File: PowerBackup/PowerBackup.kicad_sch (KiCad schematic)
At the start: 0 parts

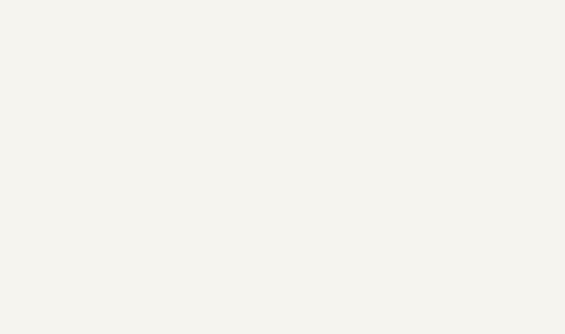
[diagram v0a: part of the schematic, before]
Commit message: Changed resistors and LEDs to 0805 and updated Production files
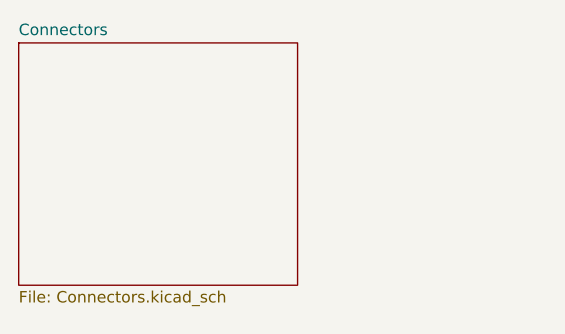
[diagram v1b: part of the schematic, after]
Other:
- added sheet Connectors (Connectors.kicad_sch)

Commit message: Did some initial board layout
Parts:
- added H1, H2, H3: MountingHole_Pad, MountingHole:MountingHole_2.7mm_M2.5_Pad, symbol Mechanical:MountingHole_Pad
- added J1: Conn_01x02_Female, Connector_JST:JST_XH_B2B-XH-A_1x02_P2.50mm_Vertical, symbol Connector:Conn_01x02_Female
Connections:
- new net +9V: J1.1 (Pin_1)
- new net GND: H1.1, H2.1, H3.1, J1.2 (Pin_2)
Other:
- removed sheet Connectors
- added sheet Backup (Backup.kicad_sch)

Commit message: Added BOM and production files
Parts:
- H1, H2, H3, J1: MFN# (none) -> -
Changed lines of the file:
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@@
     (stroke (width 0) (type default) (color 0 0 0 0))
+  )
+  (wire (pts (xy 23.876 127.762) (xy 31.242 127.762))
+    (stroke (width 0) (type default) (color 0 0 0 0))
+  )
+  (symbol (lib_id "power:PWR_FLAG") (at 23.876 127.762 0) (unit 1)
+    (in_bom yes) (on_board yes) (fields_autoplaced)
+    (property "Reference" "#FLG0101" (id 0) (at 23.876 125.857 0)
+      (effects (font (size 1.27 1.27)) hide)
+    )
+    (property "Value" "PWR_FLAG" (id 1) (at 23.876 123.19 0))
+    (property "Footprint" "" (id 2) (at 23.876 127.762 0)
+      (effects (font (size 1.27 1.27)) hide)
+    )
+    (property "Datasheet" "~" (id 3) (at 23.876 127.762 0)
+      (effects (font (size 1.27 1.27)) hide)
+    )
+    (pin "1")
   )
   (symbol (lib_id "power:GND") (at 31.242 34.29 0) (unit 1)
@@
     (pin "1")
   )
+  (symbol (lib_id "power:+9V") (at 31.242 127.762 0) (unit 1)
+    (in_bom yes) (on_board yes) (fields_autoplaced)
+    (property "Reference" "#PWR0104" (id 0) (at 31.242 131.572 0)
+      (effects (font (size 1.27 1.27)) hide)
+    )
+    (property "Value" "+9V" (id 1) (at 31.242 123.19 0))
+    (property "Footprint" "" (id 2) (at 31.242 127.762 0)
+      (effects (font (size 1.27 1.27)) hide)
+    )
+    (property "Datasheet" "" (id 3) (at 31.242 127.762 0)
+      (effects (font (size 1.27 1.27)) hide)
+    )
+    (pin "1")
+  )
   (symbol (lib_id "power:GND") (at 27.432 190.246 0) (unit 1)
     (in_bom yes) (on_board yes) (fields_autoplaced)
@@
       (effects (font (size 1.27 1.27)) hide)
     )
+    (property "MFN#" "-" (id 4) (at 34.798 186.69 0)
+      (effects (font (size 1.27 1.27)) hide)
+    )
     (pin "1")
   )
@@
       (effects (font (size 1.27 1.27)) hide)
     )
+    (property "MFN#" "-" (id 4) (at 44.196 31.496 0)
+      (effects (font (size 1.27 1.27)) hide)
+    )
     (pin "1")
     (pin "2")
@@
       (effects (font (size 1.27 1.27)) hide)
     )
+    (property "MFN#" "-" (id 4) (at 27.432 186.69 0)
+      (effects (font (size 1.27 1.27)) hide)
+    )
     (pin "1")
   )
@@
     )
     (property "Datasheet" "~" (id 3) (at 19.812 186.69 0)
+      (effects (font (size 1.27 1.27)) hide)
+    )
+    (property "MFN#" "-" (id 4) (at 19.812 186.69 0)
       (effects (font (size 1.27 1.27)) hide)
     )
@@
   )
   (symbol_instances
+    (path "/4b4f8a8e-03cf-40a7-8fad-fe39dfbabdac"
+      (reference "#FLG0101") (unit 1) (value "PWR_FLAG") (footprint "")
+    )
     (path "/68d26012-5170-4c8d-8ec1-a7d027a0af0d"
       (reference "#PWR01") (unit 1) (value "GND") (footprint "")
@@
       (reference "#PWR05") (unit 1) (value "GND") (footprint "")
     )
-    (path "/915b7dab-7a0a-46d7-be45-5545593eb525/ba36fb47-be2e-439c-8a56-c72c46503d6d"
-      (reference "#PWR06") (unit 1) (value "GNDS") (footprint "")
-    )
-    (path "/915b7dab-7a0a-46d7-be45-5545593eb525/69ac9631-ec7e-4f05-ba31-4e83c5dfbd90"
-      (reference "#PWR07") (unit 1) (value "GNDS") (footprint "")
-    )
-    (path "/915b7dab-7a0a-46d7-be45-5545593eb525/be06c08d-5421-4385-826b-8847f44af1cc"
-      (reference "#PWR08") (unit 1) (value "GNDS") (footprint "")
-    )
-    (path "/915b7dab-7a0a-46d7-be45-5545593eb525/a22b1e65-5405-474d-b1be-0a774a13d3fb"
-      (reference "#PWR09") (unit 1) (value "GNDS") (footprint "")
-    )
-    (path "/915b7dab-7a0a-46d7-be45-5545593eb525/18bf62f4-4ef8-4a56-84ab-efff4fd1d94e"
-      (reference "#PWR010") (unit 1) (value "GNDS") (footprint "")
-    )
-    (path "/915b7dab-7a0a-46d7-be45-5545593eb525/4b968b19-6208-4b08-9d76-2833cc577fde"
-      (reference "#PWR011") (unit 1) (value "GNDS") (footprint "")
-    )
-    (path "/915b7dab-7a0a-46d7-be45-5545593eb525/d05ba0a5-c00f-4110-935e-a1ec267428a9"
-      (reference "#PWR012") (unit 1) (value "GNDS") (footprint "")
-    )
     (path "/244de032-dfe4-4b77-a637-dbe4a930144c/5183010c-eb20-44ae-bdff-7b0ef9cbe2e0"
       (reference "#PWR013") (unit 1) (value "GND") (footprint "")
@@
       (reference "#PWR014") (unit 1) (value "+9VA") (footprint "")
     )
-    (path "/244de032-dfe4-4b77-a637-dbe4a930144c/982dd809-aff6-4c73-90ba-6b091ba6d3d3"
-      (reference "#PWR015") (unit 1) (value "GNDS") (footprint "")
-    )
     (path "/244de032-dfe4-4b77-a637-dbe4a930144c/c27b67c9-1c6c-4e96-bd9c-df8b06ecabfa"
       (reference "#PWR016") (unit 1) (value "GND") (footprint "")
     )
-    (path "/244de032-dfe4-4b77-a637-dbe4a930144c/0a6b7f85-dbae-4b23-ad03-dd946a99016f"
-      (reference "#PWR017") (unit 1) (value "GNDS") (footprint "")
-    )
     (path "/244de032-dfe4-4b77-a637-dbe4a930144c/4f100941-0202-412e-b25f-2426815b0ee0"
       (reference "#PWR018") (unit 1) (value "GND") (footprint "")
@@
       (reference "#PWR025") (unit 1) (value "GND") (footprint "")
     )
-    (path "/244de032-dfe4-4b77-a637-dbe4a930144c/0b29cd93-4054-4334-9a45-7f5c468b8d26"
-      (reference "#PWR026") (unit 1) (value "GNDS") (footprint "")
-    )
     (path "/244de032-dfe4-4b77-a637-dbe4a930144c/53d53a41-4add-4036-938e-8095de63bc03"
       (reference "#PWR0101") (unit 1) (value "GND") (footprint "")
@@
       (reference "#PWR0103") (unit 1) (value "GND") (footprint "")
     )
+    (path "/61304962-f808-4789-a574-6390115b0263"
+      (reference "#PWR0104") (unit 1) (value "+9V") (footprint "")
+    )
+    (path "/915b7dab-7a0a-46d7-be45-5545593eb525/a58872a1-f4df-40c9-b53f-55dfc0e96d82"
+      (reference "#PWR0105") (unit 1) (value "GND") (footprint "")
+    )
     (path "/915b7dab-7a0a-46d7-be45-5545593eb525/8f3f3f11-417f-4c06-bbcc-b50211ba0028"
       (reference "#PWR0106") (unit 1) (value "GND") (footprint "")
     )
+    (path "/915b7dab-7a0a-46d7-be45-5545593eb525/fc988c61-8c25-498a-b51f-4d1bd4e5cfdd"
+      (reference "#PWR0107") (unit 1) (value "GND") (footprint "")
+    )
+    (path "/915b7dab-7a0a-46d7-be45-5545593eb525/df071463-1984-468d-abfe-2ebfe4e0290d"
+      (reference "#PWR0108") (unit 1) (value "GND") (footprint "")
+    )
+    (path "/915b7dab-7a0a-46d7-be45-5545593eb525/36232c92-8f9c-4be8-a6ed-e75aaa5aafb1"
+      (reference "#PWR0109") (unit 1) (value "GND") (footprint "")
+    )
+    (path "/915b7dab-7a0a-46d7-be45-5545593eb525/11e63992-5552-44b5-a7fb-acf18c1d80b3"
+      (reference "#PWR0110") (unit 1) (value "GND") (footprint "")
+    )
+    (path "/915b7dab-7a0a-46d7-be45-5545593eb525/20e2ec52-af06-4ab2-bab6-143ad91599db"
+      (reference "#PWR0111") (unit 1) (value "GND") (footprint "")
+    )
     (path "/244de032-dfe4-4b77-a637-dbe4a930144c/c1afdbbf-457f-46e1-8740-4c0cb8fc4e40"
       (reference "#PWR0112") (unit 1) (value "+9V") (footprint "")
@@
       (reference "#PWR0113") (unit 1) (value "+9VA") (footprint "")
     )
+    (path "/915b7dab-7a0a-46d7-be45-5545593eb525/7ca22684-f376-4027-98c3-6a7b6495bdd6"
+      (reference "#PWR0114") (unit 1) (value "GND") (footprint "")
+    )
+    (path "/244de032-dfe4-4b77-a637-dbe4a930144c/628c3a84-b501-4396-af63-e0fb27482409"
+      (reference "#PWR0115") (unit 1) (value "GND") (footprint "")
+    )
+    (path "/244de032-dfe4-4b77-a637-dbe4a930144c/1f38873a-2904-49d7-9cf8-59e753c29493"
+      (reference "#PWR0116") (unit 1) (value "GND") (footprint "")
+    )
+    (path "/244de032-dfe4-4b77-a637-dbe4a930144c/abee4203-8fa1-4170-92ac-e1de669bd2f6"
+      (reference "#PWR0117") (unit 1) (value "GND") (footprint "")
+    )
     (path "/915b7dab-7a0a-46d7-be45-5545593eb525/b8789d48-2b31-4570-a6f4-71b97923d578"
       (reference "C1") (unit 1) (value "1u") (footprint "Capacitor_SMD:C_0603_1608Metric")
@@
     )
     (path "/915b7dab-7a0a-46d7-be45-5545593eb525/eddbd4cc-03db-45bd-a7b8-4c72f079a2b7"
-      (reference "R9") (unit 1) (value "1k") (footprint "Resistor_SMD:R_0805_2012Metric")
+      (reference "R9") (unit 1) (value "1k") (footprint "Resistor_SMD:R_0603_1608Metric")
     )
     (path "/915b7dab-7a0a-46d7-be45-5545593eb525/77ca280f-43a5-4095-85d6-5d01ef62aa4c"
@@
     )
     (path "/915b7dab-7a0a-46d7-be45-5545593eb525/d4d364f2-a99e-4857-ab65-e8c137b15a1a"
-      (reference "R12") (unit 1) (value "1k") (footprint "Resistor_SMD:R_0805_2012Metric")
+      (reference "R12") (unit 1) (value "1k") (footprint "Resistor_SMD:R_0603_1608Metric")
     )
     (path "/915b7dab-7a0a-46d7-be45-5545593eb525/3d824368-3035-4a76-813c-33efd3bccdb7"
@@
     )
     (path "/915b7dab-7a0a-46d7-be45-5545593eb525/6f3e3f7e-ff3d-48b7-9ddc-5aeef4671a66"
-      (reference "R14") (unit 1) (value "200") (footprint "Resistor_SMD:R_0805_2012Metric")
+      (reference "R14") (unit 1) (value "100") (footprint "Resistor_SMD:R_0805_2012Metric")
     )
     (path "/915b7dab-7a0a-46d7-be45-5545593eb525/67b97d21-9684-4377-ad59-a035ca7da75a"
@@
     )
     (path "/244de032-dfe4-4b77-a637-dbe4a930144c/54a4ee77-1f30-46ae-ae06-cd0f517c898a"
-      (reference "R18") (unit 1) (value "1.5k") (footprint "Resistor_SMD:R_0603_1608Metric")
+      (reference "R18") (unit 1) (value "1k") (footprint "Resistor_SMD:R_0603_1608Metric")
     )
     (path "/244de032-dfe4-4b77-a637-dbe4a930144c/8818e700-28bf-4f3a-b208-8b210bffc041"
@@
       (reference "R23") (unit 1) (value "30k") (footprint "Resistor_SMD:R_0603_1608Metric")
     )
+    (path "/915b7dab-7a0a-46d7-be45-5545593eb525/204e421e-7eaf-4cb3-86fa-d9499c7c1b1a"
+      (reference "R24") (unit 1) (value "100") (footprint "Resistor_SMD:R_0805_2012Metric")
+    )
     (path "/915b7dab-7a0a-46d7-be45-5545593eb525/7502ade2-8dff-4682-9787-9a2c2e5dc707"
-      (reference "TH1") (unit 1) (value "Thermistor_NTC") (footprint "Resistor_SMD:R_0805_2012Metric")
+      (reference "TH1") (unit 1) (value "10k") (footprint "Resistor_SMD:R_0805_2012Metric")
     )
     (path "/915b7dab-7a0a-46d7-be45-5545593eb525/4854008c-3227-404e-9125-8acbd6988fad"
